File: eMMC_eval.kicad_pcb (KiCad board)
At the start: 2 copper layers, 71.1 x 35.6 mm, 10 parts, among them J1 Conn_01x03_Male, J2 Conn_01x04_Male, J3 Conn_01x10_Male, J4 eMMC Module, J5 Conn_01x03_Male, J6 Conn_01x03_Male, J7 Conn_01x10_Male, J8 Conn_01x05_Male, J9 Conn_01x05_Male

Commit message: WIP before back-annotation test
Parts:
- removed the J4 at (137.2, 103.5)
- removed J7: Conn_01x10_Male, Connector_PinSocket_2.54mm:PinSocket_1x10_P2.54mm_Vertical
- removed J8, J9: Conn_01x05_Male, Connector_PinHeader_2.54mm:PinHeader_1x05_P2.54mm_Vertical
- removed JP1: SolderJumper_2_Bridged, Jumper:SolderJumper-2_P1.3mm_Bridged_RoundedPad1.0x1.5mm
- added C1: 2.2uF 6.3V, Capacitor_SMD:C_0603_1608Metric, F.Cu at (170.2, 102.9)
- added J6: Conn_01x04_Male, Connector_PinSocket_2.54mm:PinSocket_1x04_P2.54mm_Vertical, B.Cu at (179.3, 116.5)
- added U1: THGBMNG5D1LBAIT, Kicad_Footprints:BGA153N50P14X14_1000X1100X80, F.Cu at (160.4, 101.4)
- J4: renamed from J5; footprint Connector_PinHeader_2.54mm:PinHeader_1x03_P2.54mm_Vertical -> Connector_PinSocket_2.54mm:PinSocket_1x03_P2.54mm_Vertical; moved to B.Cu
- J5: renamed from J6; value Conn_01x03_Male -> Conn_01x10_Male; footprint Connector_PinSocket_2.54mm:PinSocket_1x03_P2.54mm_Vertical -> Connector_PinSocket_2.54mm:PinSocket_1x10_P2.54mm_Vertical
- moved J4 22.0 mm to (188.0, 96.5), turned to 180 degrees
- moved J3 15.2 mm to (170.7, 114.0)
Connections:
- J2 pad 3: Net-(J2-Pad3) -> /~SDMMC1_RST
- J4 pad 1: /STRB -> /SDMMC1_D0
- J4 pad 2: /RESET -> /SDMMC1_D6
- J4 pad 3: GND -> (no net)
- J5 pad 1: /SDMMC1_D0 -> /SDMMC1_D1
- J5 pad 2: /SDMMC1_D6 -> /SDMMC1_D4
- J5 pad 3: Net-(J6-Pad3) -> /SDMMC1_D5
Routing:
- net /STRB: track 81.8 -> 0.00 mm, vias 5 -> 0
- net /RESET: track 73.5 -> 0.00 mm, vias 5 -> 0
- net +3V3: track 63.6 -> 6.63 mm, vias 1 -> 5
- net /SDMMC1_D4: track 91.6 -> 45.1 mm, vias 5 -> 3
- net /RESET_x: track 41.6 -> 0.00 mm, vias 1 -> 0
- net /STRB_x: track 35.4 -> 0.00 mm
- net /~SDMMC1_RST: track 0.00 -> 33.4 mm
- net /SDMMC1_D0: track 78.1 -> 45.0 mm, vias 3 -> 2
- net /SDMMC1_D6: track 79.7 -> 52.4 mm
- net /SDMMC1_CK: track 49.4 -> 73.8 mm
- net /SDMMC1_CMD: track 50.2 -> 71.4 mm, vias 3 -> 2
- net /~SPI1-NSS: track 0.00 -> 19.2 mm, vias 0 -> 2
- net GND: track 0.00 -> 18.4 mm, vias 0 -> 8
- net /SDMMC1_D1: track 69.0 -> 53.3 mm
- net /SPI1-MOSI: track 0.00 -> 12.1 mm
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- added copper zone on 3V3, net +3V3
- added copper zone on GND, net GND
- removed copper zone on F.Cu, net GND
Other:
- copper layers 2 -> 4
- net class Default: clearance 0.2 -> 0.0889; trace_width 0.25 -> 0.0889; via_dia 0.8 -> 0.3556; via_drill 0.4 -> 0.254
- rule pad_to_mask_clearance: 0.0508 -> 0.0254
- rule trace_clearance: 0.2 -> 0.0889
- rule trace_min: 0.2 -> 0.0762
- rule via_min_drill: 0.3 -> 0.127
- rule via_min_size: 0.4 -> 0.2794
- board text removed: "VCC_IO"
- board text removed: "eMMC Module"

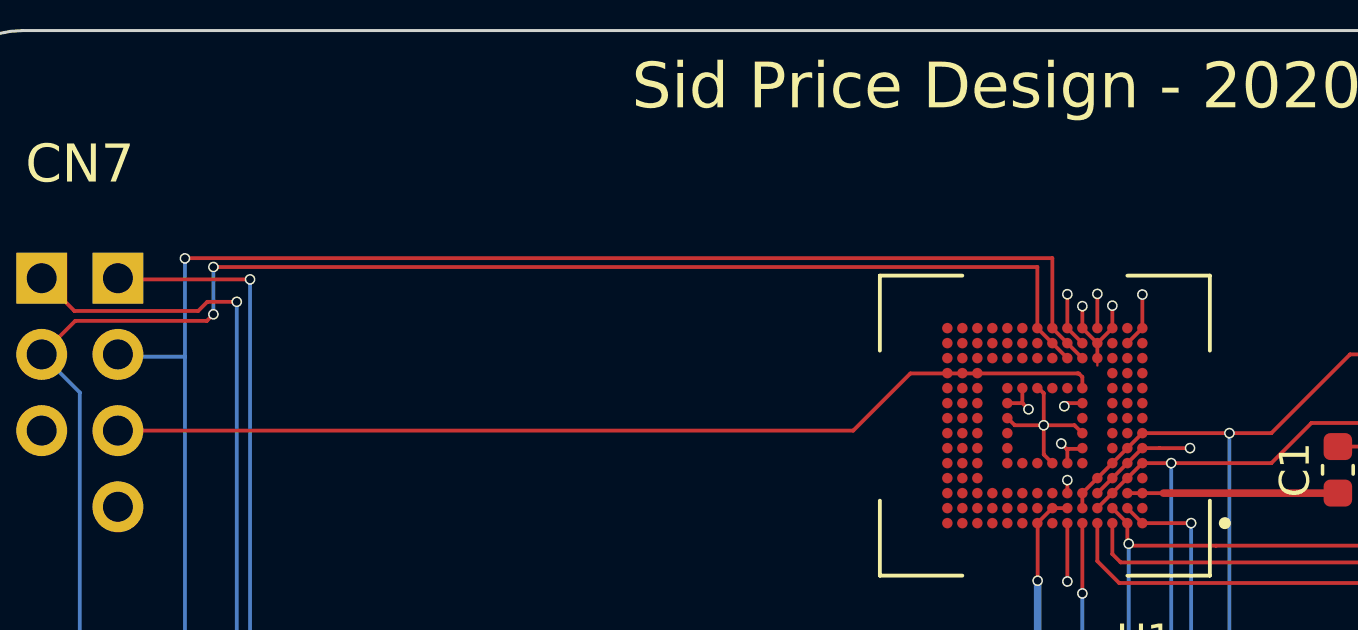
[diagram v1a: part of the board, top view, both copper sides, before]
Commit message: Back annotate #1
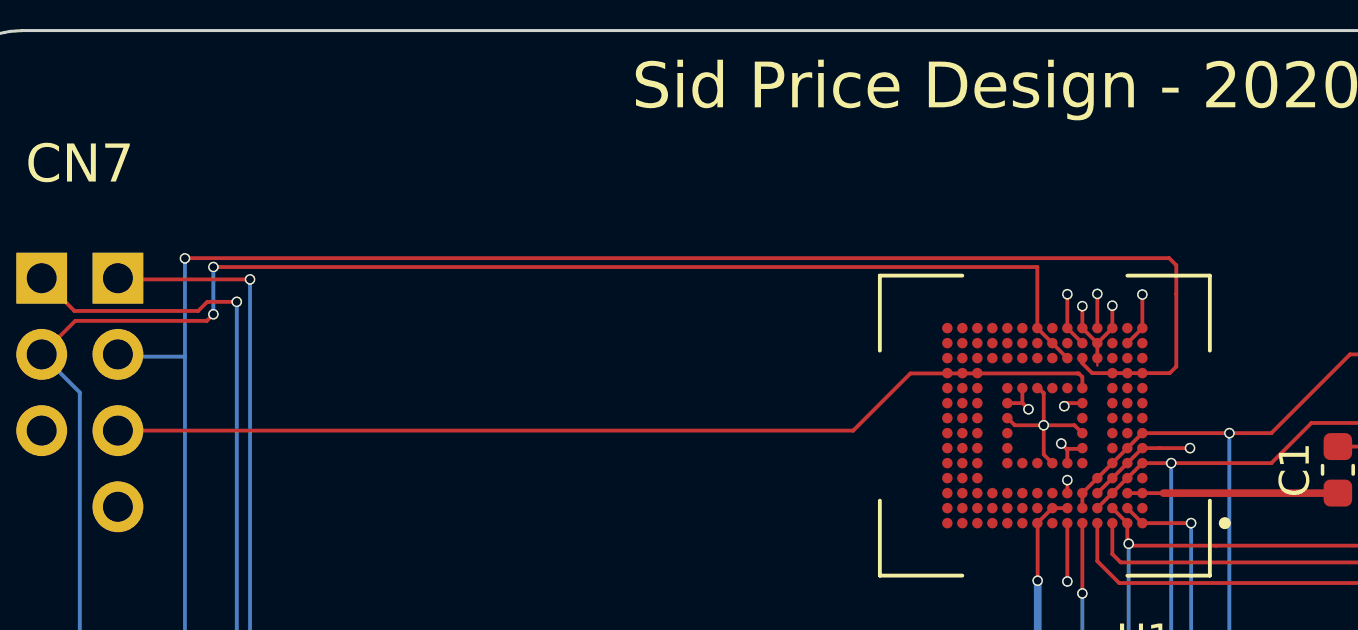
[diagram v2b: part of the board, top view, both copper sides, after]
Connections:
- U1 pad L1: (no net) -> /SDMMC1_CMD
- U1 pad L2: (no net) -> /SDMMC1_CMD
- U1 pad L3: (no net) -> /SDMMC1_CMD
- U1 pad N6: /SDMMC1_CMD -> (no net)
- U1 pad P7: /SDMMC1_CMD -> (no net)
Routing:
- net /SDMMC1_CMD: track 71.4 -> 78.8 mm

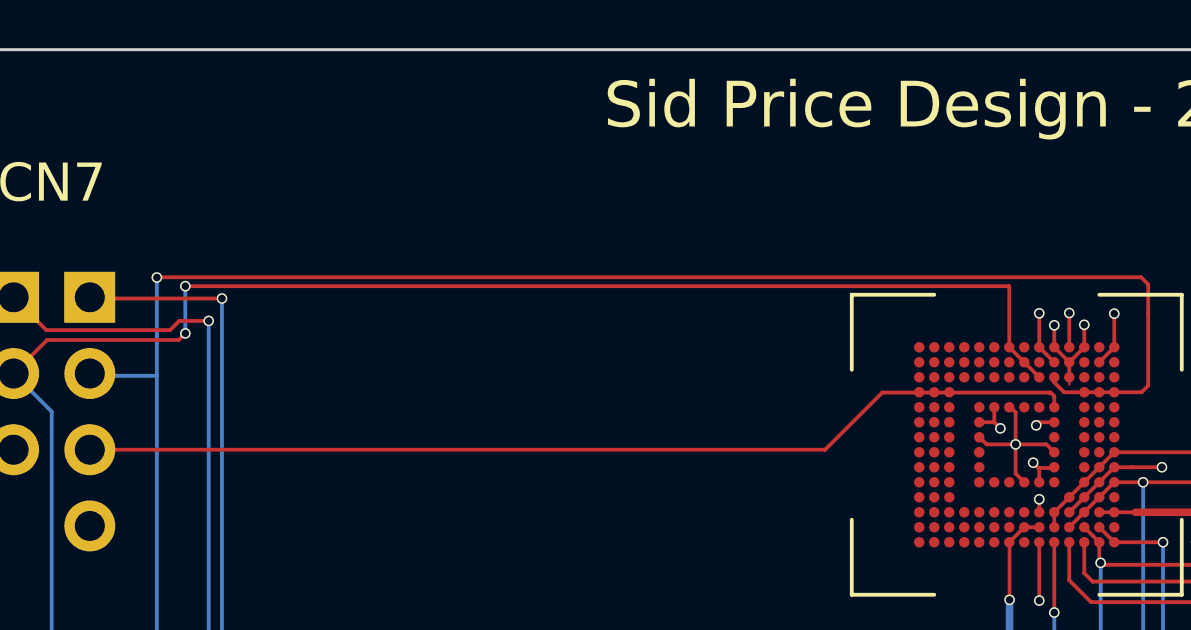
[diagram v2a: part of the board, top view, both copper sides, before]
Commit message: eMMC chip symbol updated and pushed to PCB
Has all NC pins remapped to the signals the PCB needs to use to escape the BGA
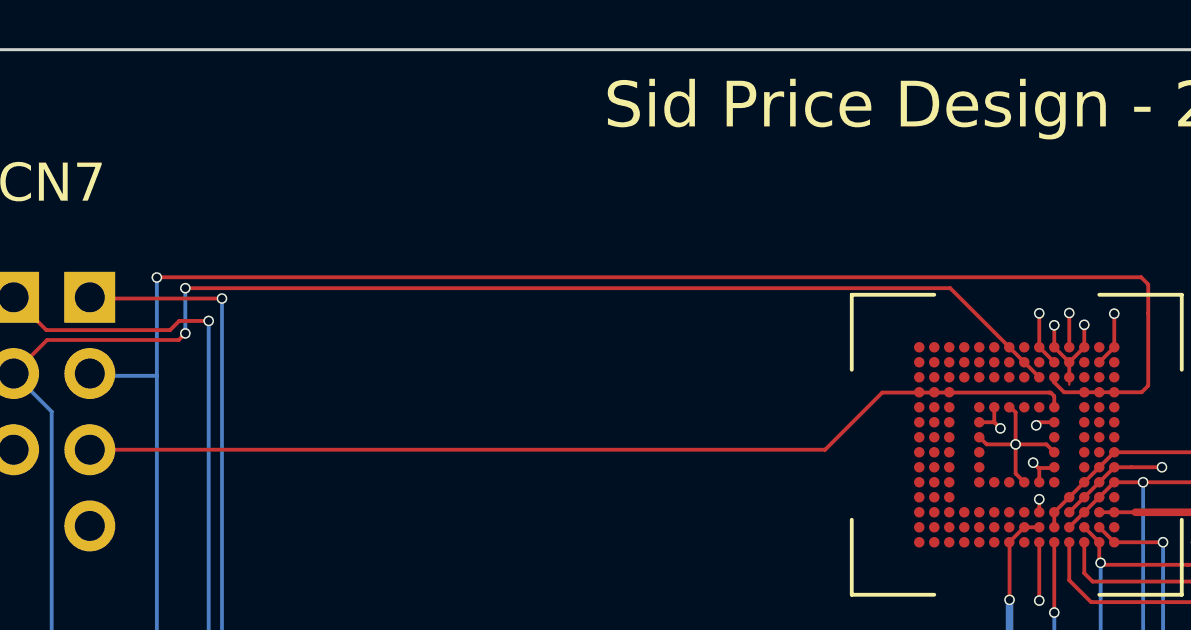
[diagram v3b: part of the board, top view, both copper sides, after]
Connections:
- U1 pad C1: (no net) -> Net-(C1-Pad1)
- U1 pad N6: (no net) -> /SDMMC1_CMD
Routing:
- net /SDMMC1_CK: track 73.8 -> 72.5 mm

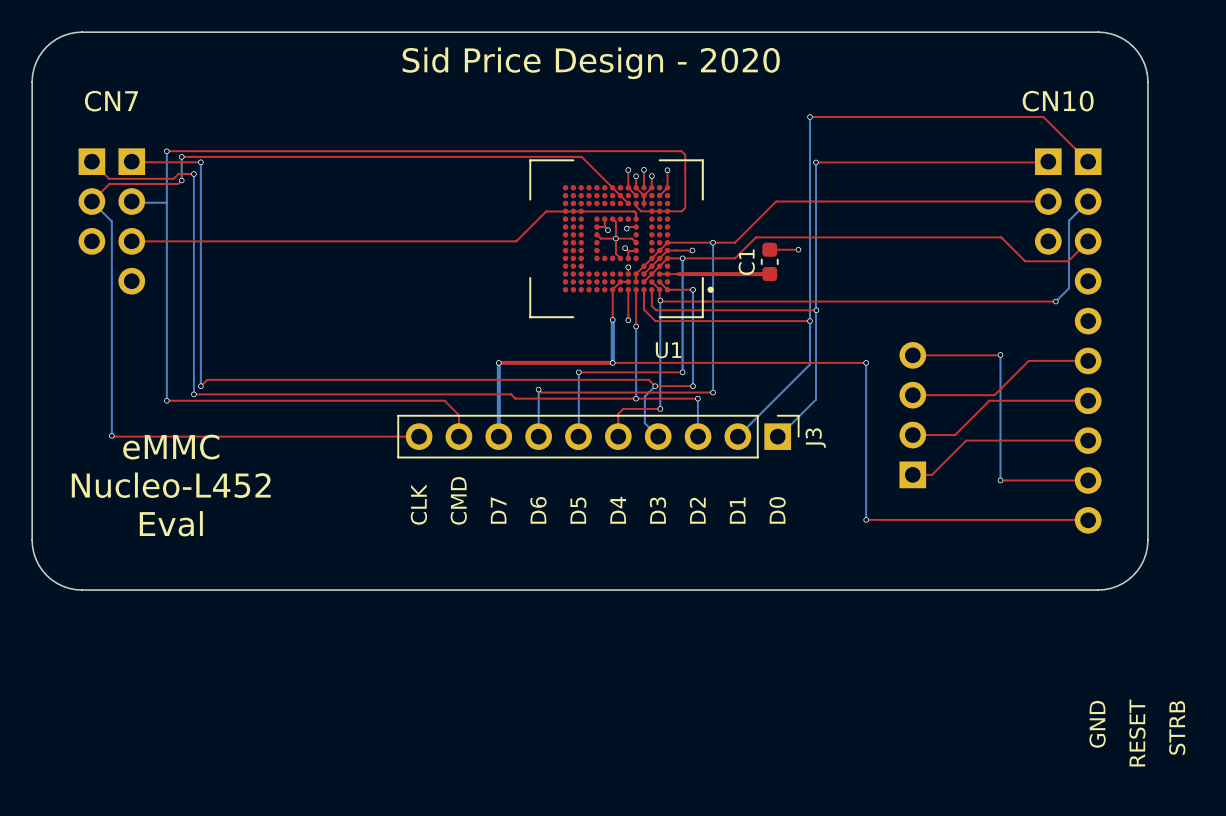
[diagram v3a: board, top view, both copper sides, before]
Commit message: Increase track widths where possible
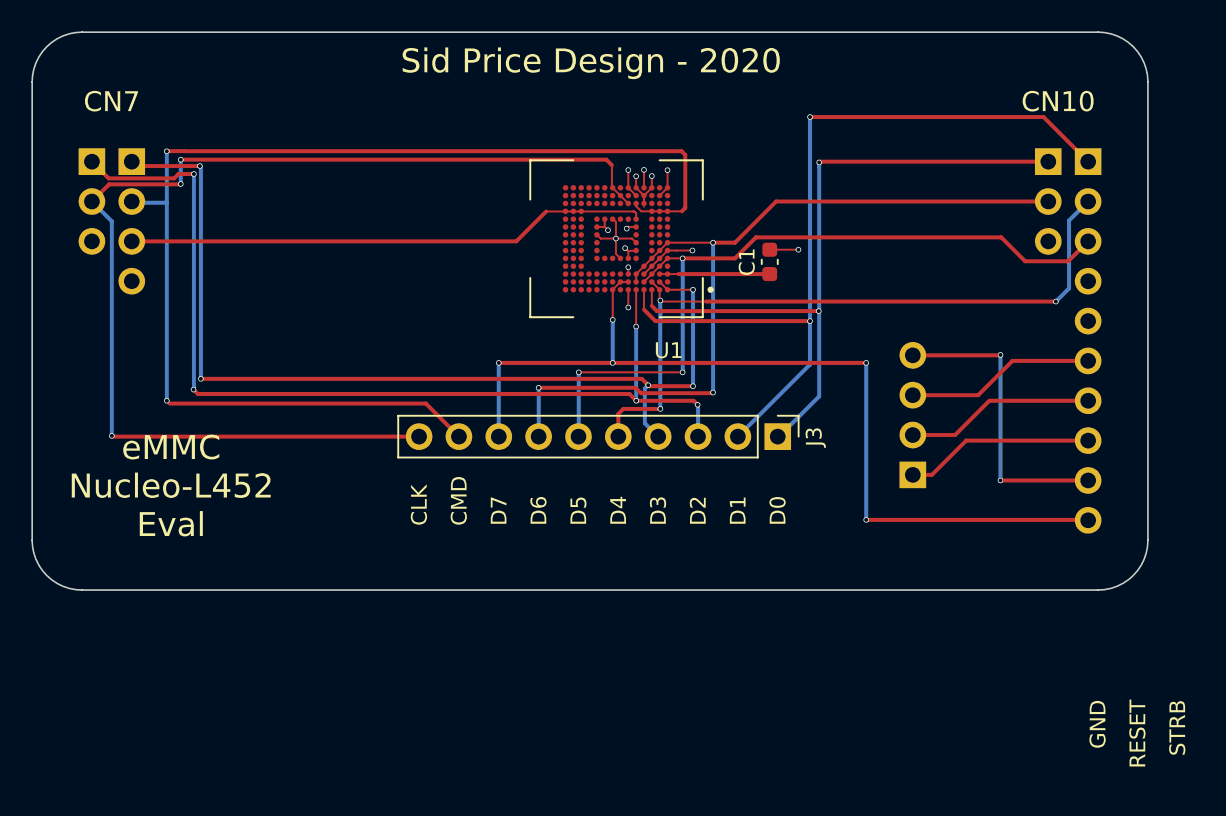
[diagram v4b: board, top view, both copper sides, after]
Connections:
- U1 pad N6: /SDMMC1_CMD -> (no net)
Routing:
- net /SDMMC1_D3: track 62.7 -> 61.8 mm
- net GND: track 18.4 -> 17.6 mm
- net /SDMMC1_CMD: track 78.8 -> 78.0 mm
- net /SDMMC1_CK: track 72.5 -> 73.2 mm

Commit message: Fixed SPI header to be pins, added 3D model for eMMC
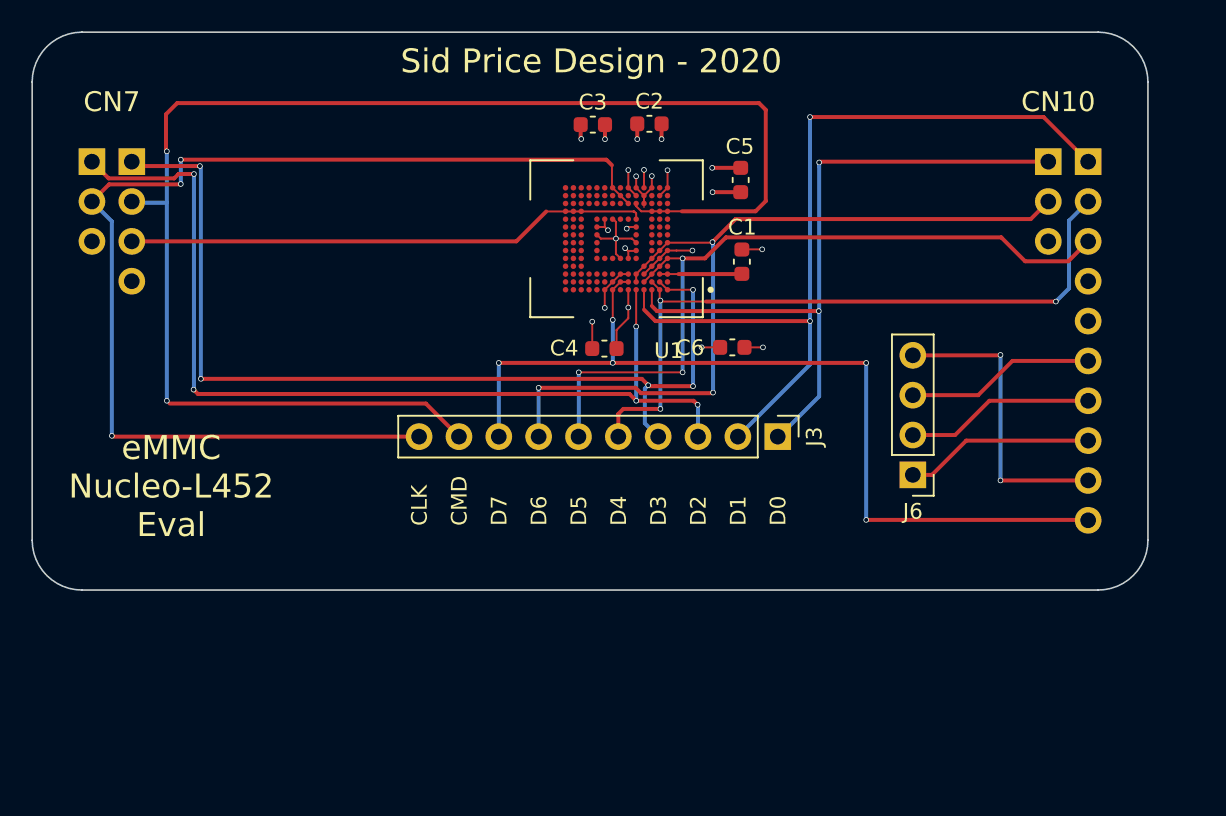
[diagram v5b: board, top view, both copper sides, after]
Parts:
- added C2: 10uF 10V, Capacitor_SMD:C_0603_1608Metric, F.Cu at (162.5, 94.1)
- added C3: 100nF, Capacitor_SMD:C_0603_1608Metric, F.Cu at (158.9, 94.2)
- added C4: 100nF, Capacitor_SMD:C_0603_1608Metric, F.Cu at (159.7, 108.4)
- added C5: 100nF, Capacitor_SMD:C_0603_1608Metric, F.Cu at (168.4, 97.7)
- added C6: 100nF, Capacitor_SMD:C_0603_1608Metric, F.Cu at (167.8, 108.4)
- J6: footprint Connector_PinSocket_2.54mm:PinSocket_1x04_P2.54mm_Vertical -> Connector_PinHeader_2.54mm:PinHeader_1x04_P2.54mm_Vertical; moved to F.Cu
- moved C1 1.78 mm to (168.4, 102.9)
- turned J6 to 180 degrees
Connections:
- U1 pad A9: (no net) -> +3V3
- U1 pad B8: (no net) -> +3V3
- U1 pad C7: (no net) -> +3V3
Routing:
- net /SDMMC1_CMD: track 78.0 -> 93.6 mm
- net +3V3: track 6.63 -> 15.9 mm, vias 5 -> 10
- net GND: track 17.6 -> 24.9 mm, vias 8 -> 12
- net Net-(C1-Pad1): track 7.02 -> 5.25 mm
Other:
- board text removed: "GND"
- board text removed: "RESET"
- board text removed: "STRB"
